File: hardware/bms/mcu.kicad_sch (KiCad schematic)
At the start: 16 parts

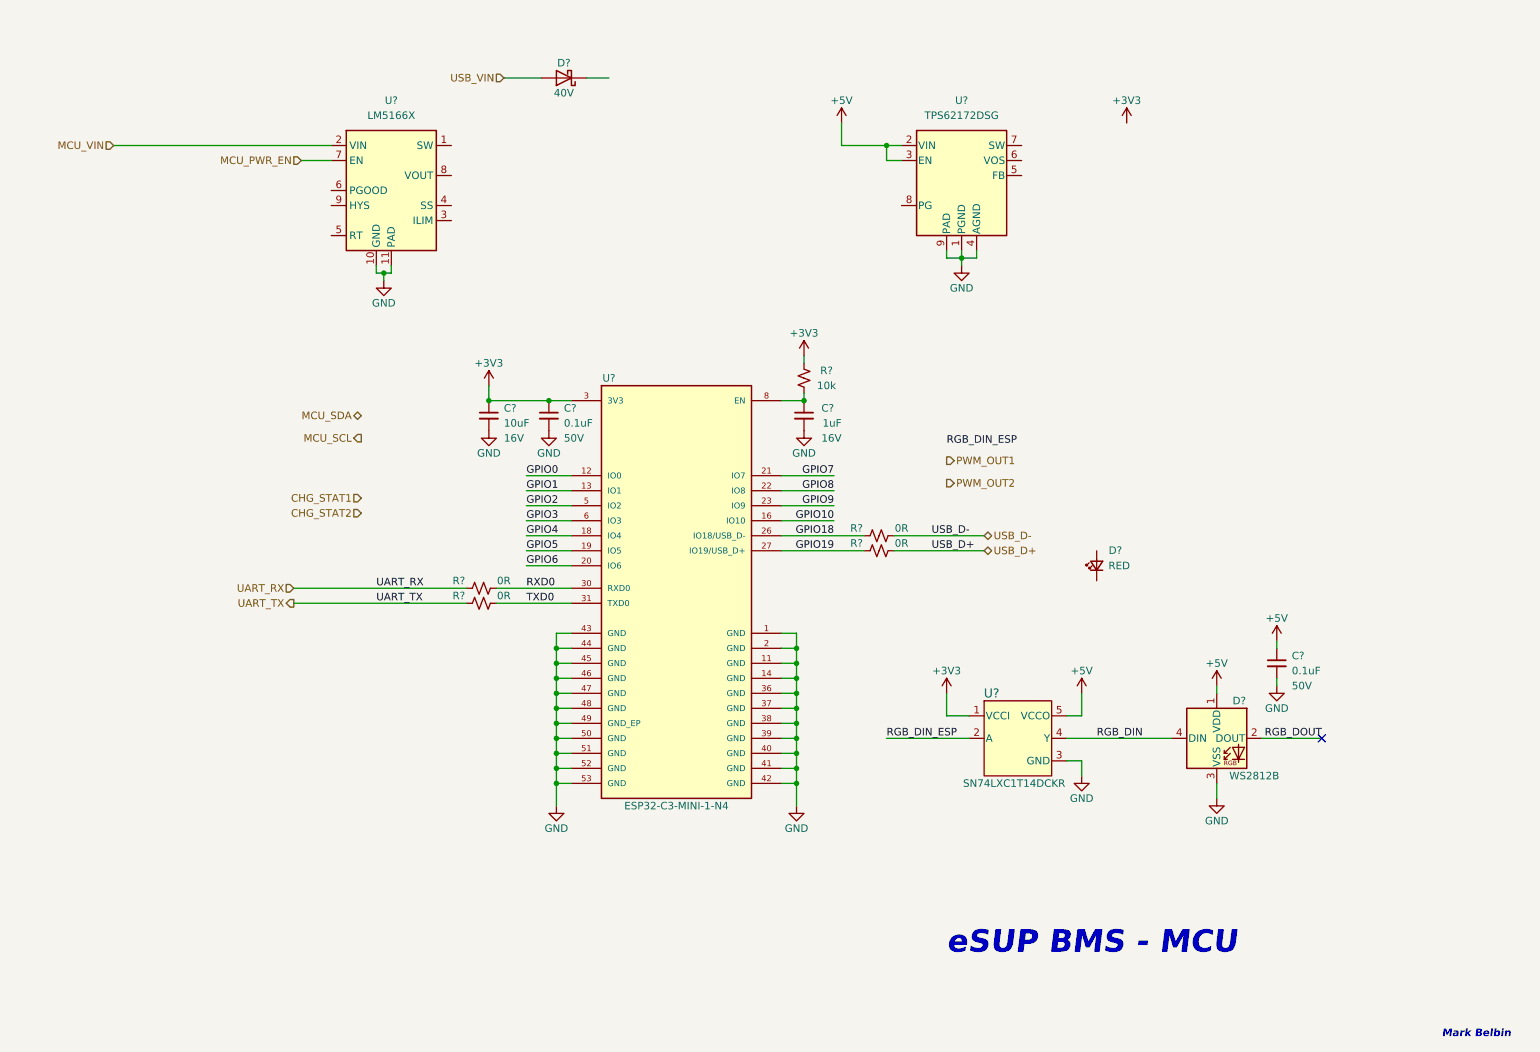
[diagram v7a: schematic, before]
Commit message: MCU power conversion section complete
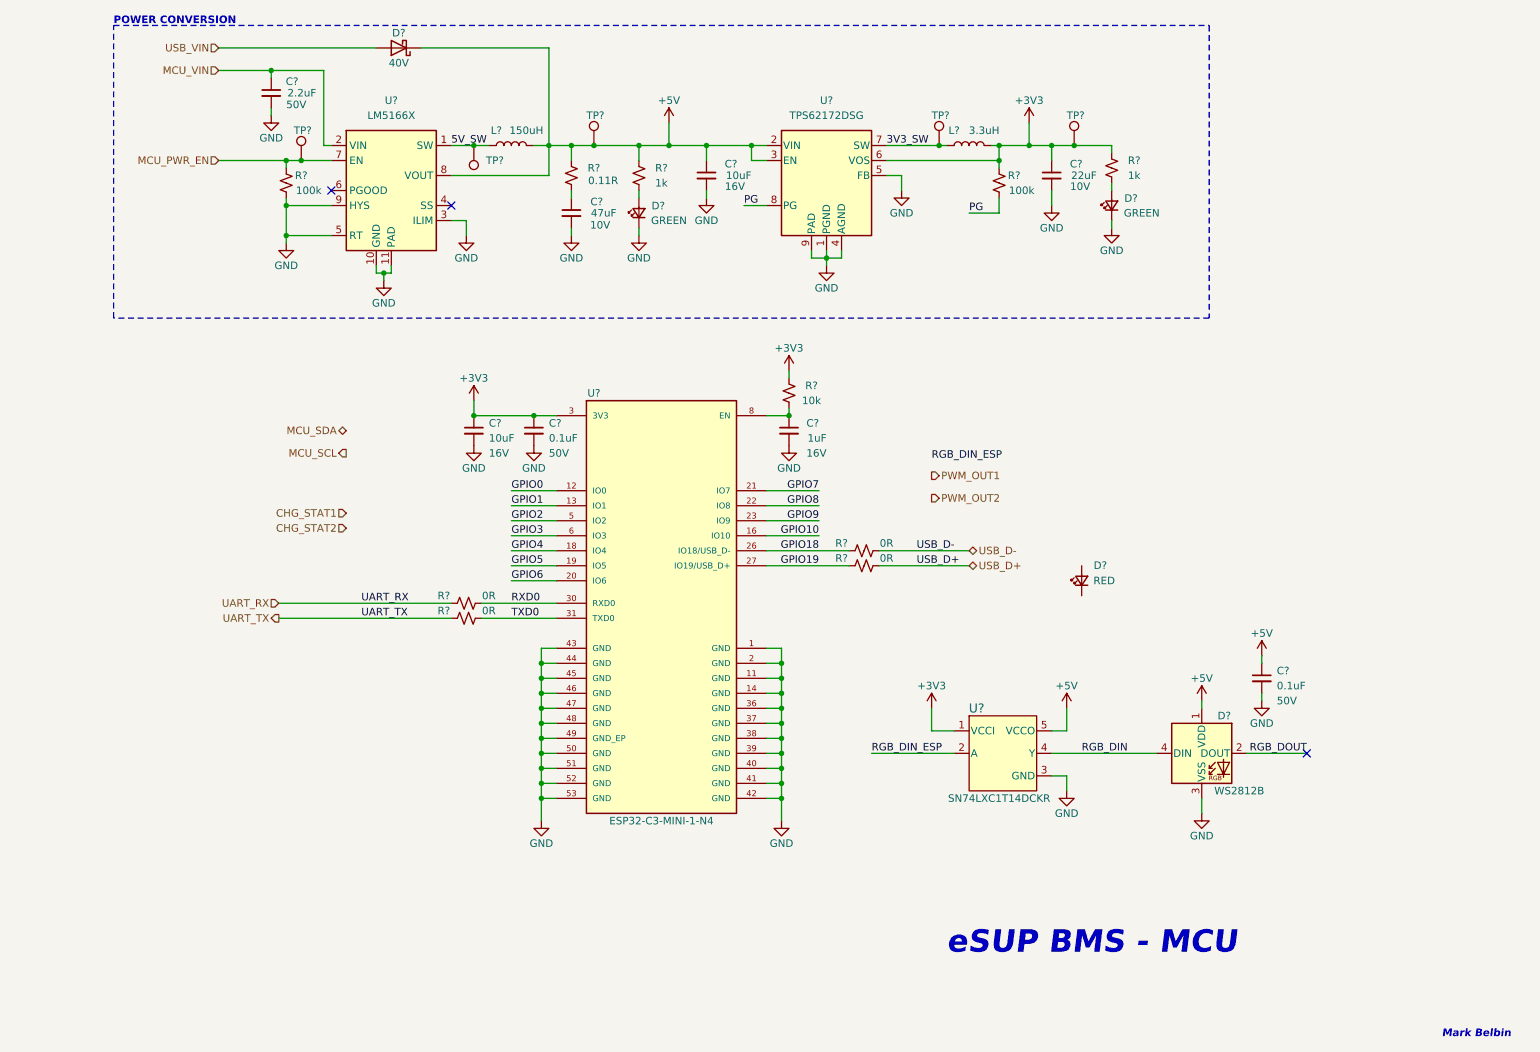
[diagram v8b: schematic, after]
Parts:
- added C?: 2.2uF, Capacitor_SMD:C_1206_3216Metric, symbol Device:C_Small
- added C?: 22uF, Capacitor_SMD:C_0805_2012Metric, symbol Device:C_Small
- added C?: 10uF, Capacitor_SMD:C_0805_2012Metric, symbol Device:C_Small
- added C?: 47uF, Capacitor_SMD:C_1210_3225Metric, symbol Device:C_Small
- added D? (x2): GREEN, LED_SMD:LED_0603_1608Metric, symbol Device:LED_Small
- added L?: 3.3uH, symbol Device:L
- added L?: 150uH, bms:IND_1050P-WE-PD_WRE-L, symbol Device:L
- added R?: 0.11R, Resistor_SMD:R_0603_1608Metric, symbol Device:R_Small_US
- added R? (x2): 1k, Resistor_SMD:R_0603_1608Metric, symbol Device:R_Small_US
- added R? (x2): 100k, Resistor_SMD:R_0603_1608Metric, symbol Device:R_Small_US
- added TP? (x5): TestPoint, TestPoint:TestPoint_Pad_D1.0mm, symbol Connector:TestPoint
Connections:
- net +3V3: now also U?.6 (VOS), C?.1, L?.2, R?.2, R?.2, TP?.1
- net +5V: now also D?.1 (K), U?.8 (VOUT), C?.1, L?.2, R?.2, R?.2, TP?.1
- net GND: now also U?.3 (ILIM), U?.5 (FB), U?.5 (RT), U?.9 (HYS), C?.2, C?.2, C?.2, C?.2, D?.1 (K), D?.1 (K), R?.1
- net MCU_PWR_EN: now also R?.2, TP?.1
- net MCU_VIN: now also C?.1
- net 5V_SW: now reaches U?.1 (SW)
- net 5V_SW: now also L?.1, TP?.1
- net 3V3_SW: now reaches U?.7 (SW)
- net 3V3_SW: now also L?.1, TP?.1
- net PG: now reaches U?.8 (PG)
- net PG: now also R?.1
- new net: C?.1, R?.1
- new net: D?.2 (A), R?.1 (x2)
- no-connect marks 1 -> 3
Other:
- note added: "POWER CONVERSION"
- moved on the sheet: C?, D?, R?, U?
